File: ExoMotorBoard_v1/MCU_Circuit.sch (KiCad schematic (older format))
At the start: 11 parts, among them IC1 DSPIC33FJ128MC802-I_SP, SW1 SW_Push_Dual

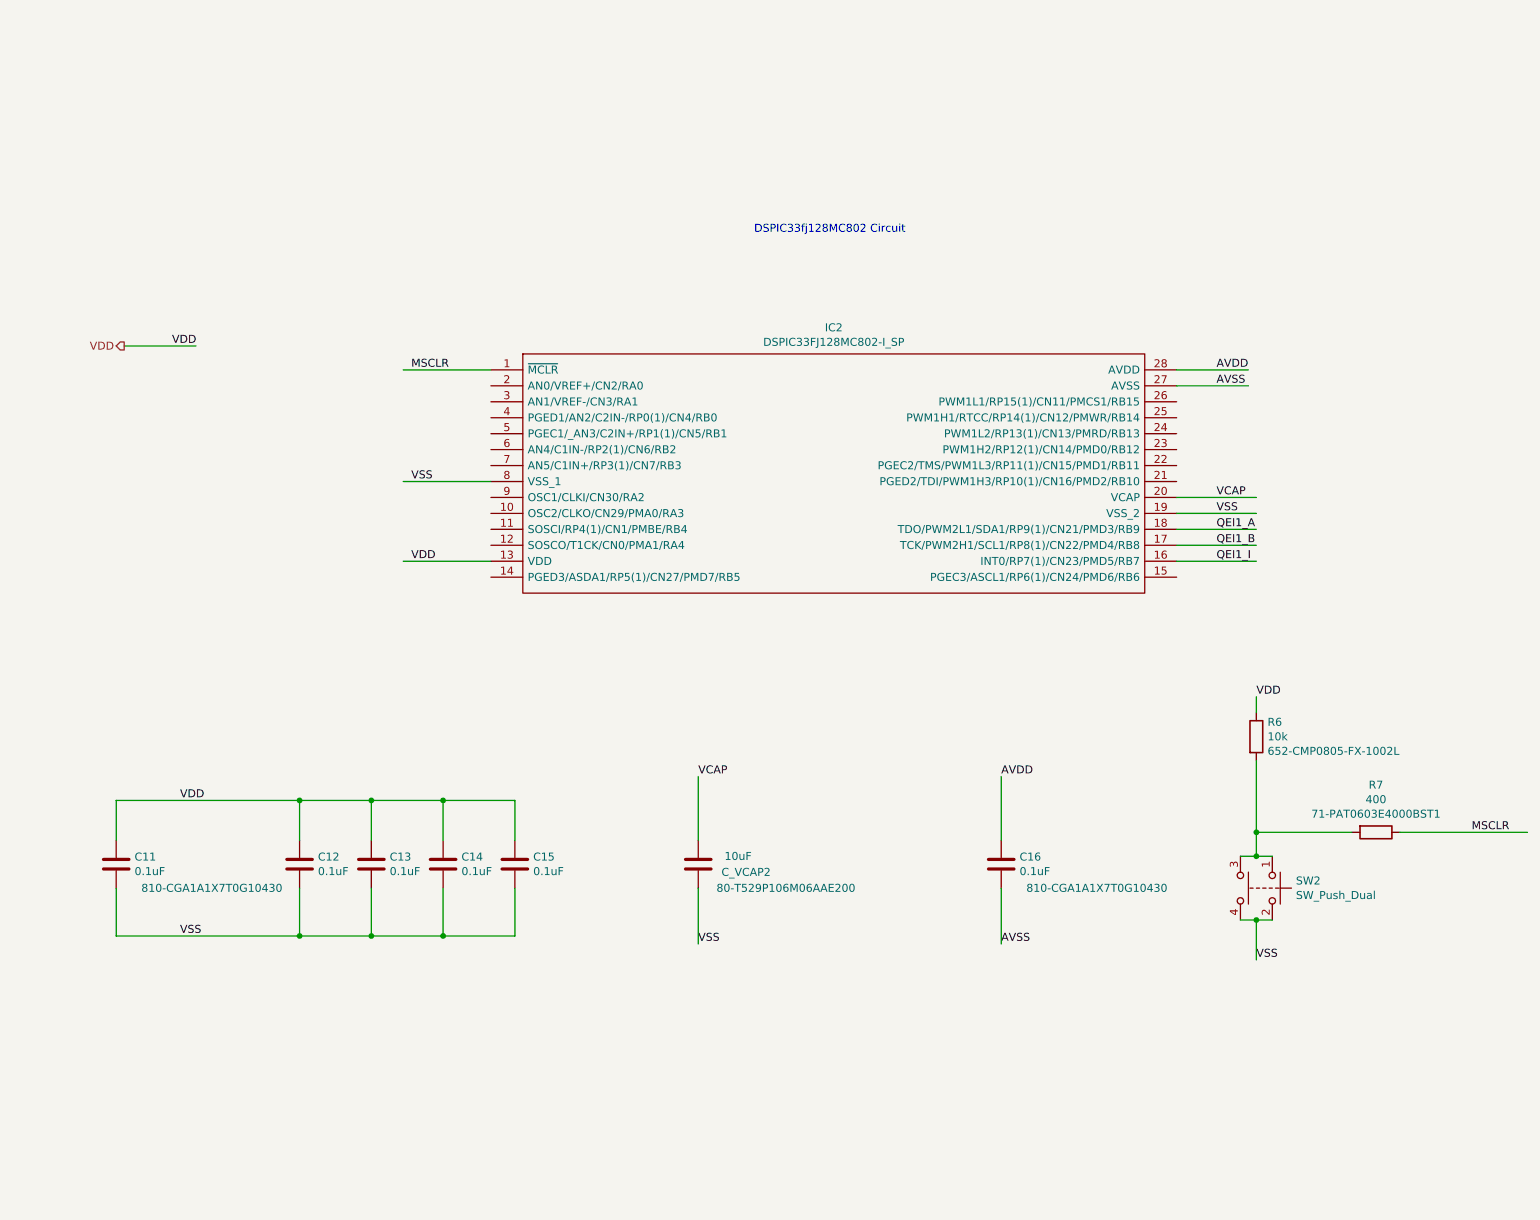
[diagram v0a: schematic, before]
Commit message: MCU schematic connections updated
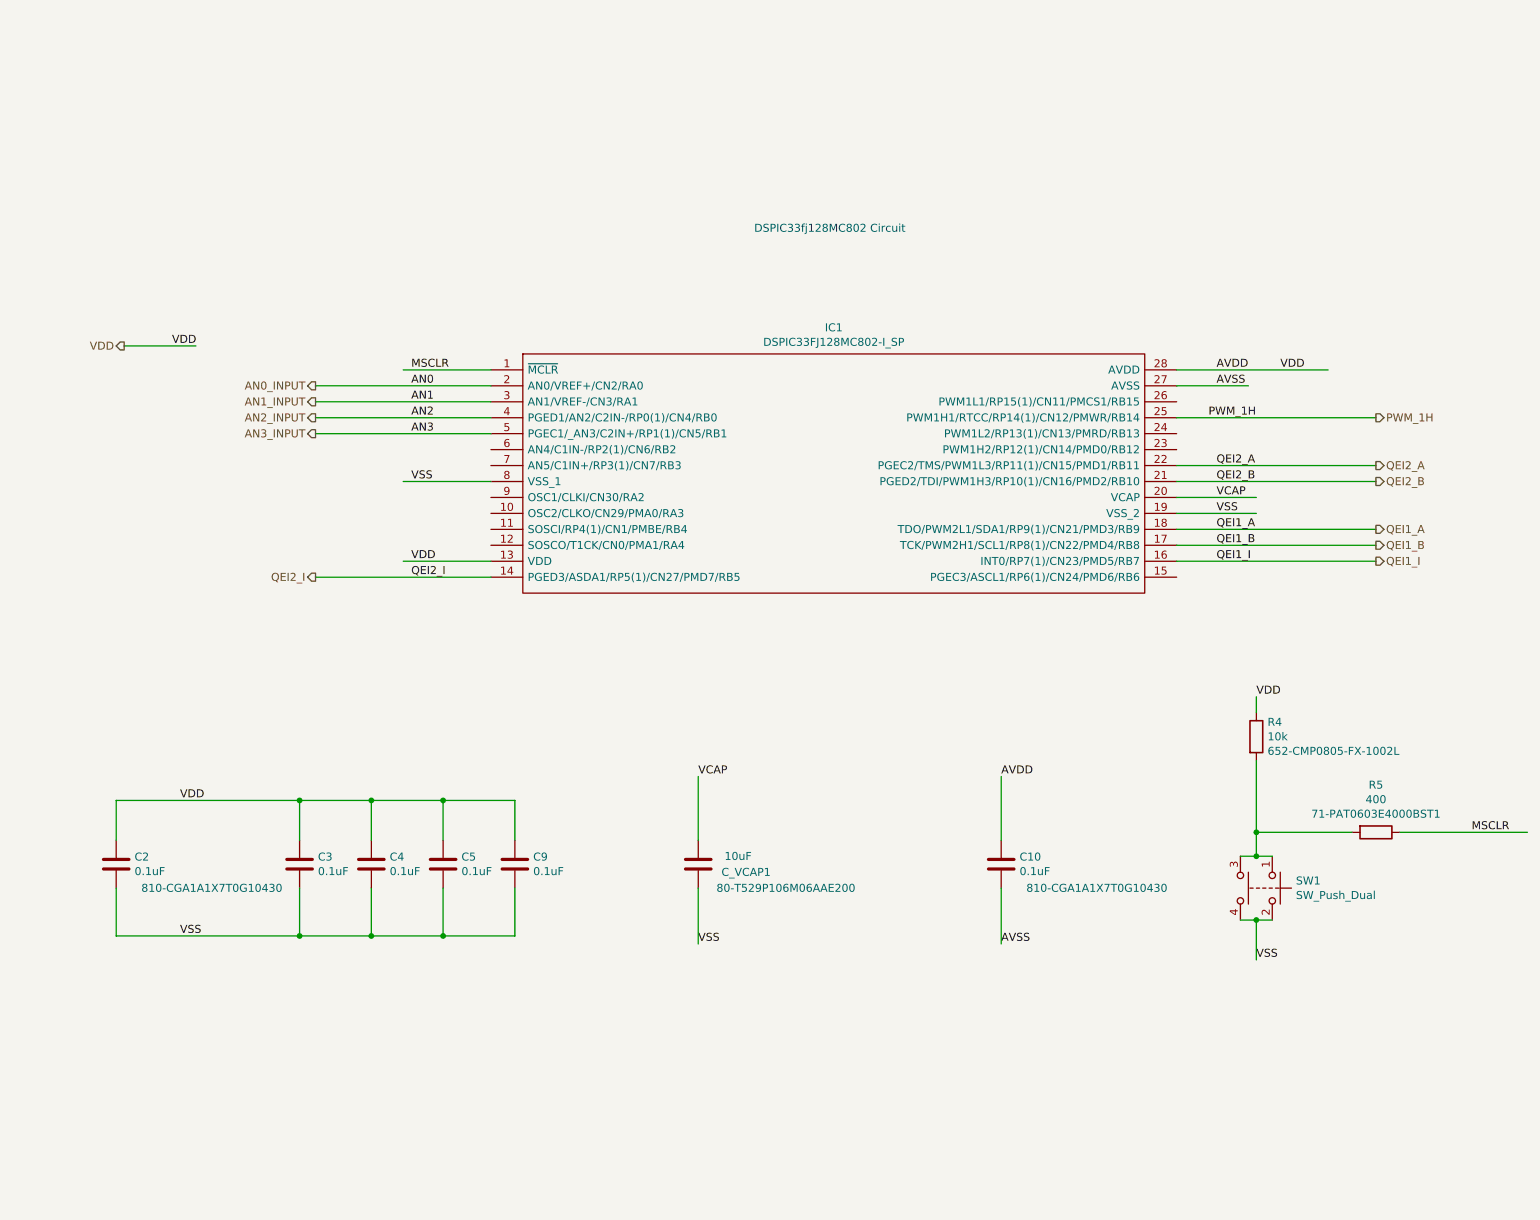
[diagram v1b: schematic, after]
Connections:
- net labels added: AN0, AN0_INPUT, AN1, AN1_INPUT, AN2, AN2_INPUT, AN3, AN3_INPUT, PWM_1H, QEI2_A, QEI2_B, QEI2_I
- wire segments 43 -> 51
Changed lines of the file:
@@
 $Descr A4 11693 8268
 encoding utf-8
-Sheet 8 8
+Sheet 2 8
 Title ""
 Date ""
@@
 AR Path="/610E570F/610E8175" Ref="IC1"  Part="1"
 AR Path="/6118F320/610E8175" Ref="IC2"  Part="1"
-F 0 "IC2" H 5950 2615 50  0000 C CNN
+F 0 "IC1" H 5950 2615 50  0000 C CNN
 F 1 "DSPIC33FJ128MC802-I_SP" H 5950 2524 50  0000 C CNN
 F 2 "DSPIC33FJ128MC802-I_SP:DIP794W56P254L3486H508Q28N" H 7950 2450 50  0001 L CNN
@@
 AR Path="/610E570F/610E817B" Ref="C_VCAP1"  Part="1"
 AR Path="/6118F320/610E817B" Ref="C_VCAP2"  Part="1"
-F 0 "C_VCAP2" H 4800 5500 50  0000 C CNN
+F 0 "C_VCAP1" H 4800 5500 50  0000 C CNN
 F 1 "10uF" H 4850 5400 50  0000 C CNN
 F 2 "Capacitor_SMD:C_0805_2012Metric_Pad1.18x1.45mm_HandSolder" H 5138 5300 50  0001 C CNN
@@
 AR Path="/610E570F/610E818F" Ref="C2"  Part="1"
 AR Path="/6118F320/610E818F" Ref="C11"  Part="1"
-F 0 "C11" H 1565 5496 50  0000 L CNN
+F 0 "C2" H 1565 5496 50  0000 L CNN
 F 1 "0.1uF" H 1565 5405 50  0000 L CNN
 F 2 "Capacitor_SMD:C_0805_2012Metric_Pad1.18x1.45mm_HandSolder" H 1488 5300 50  0001 C CNN
@@
 AR Path="/610E570F/61167308" Ref="C3"  Part="1"
 AR Path="/6118F320/61167308" Ref="C12"  Part="1"
-F 0 "C12" H 2715 5496 50  0000 L CNN
+F 0 "C3" H 2715 5496 50  0000 L CNN
 F 1 "0.1uF" H 2715 5405 50  0000 L CNN
 F 2 "Capacitor_SMD:C_0805_2012Metric_Pad1.18x1.45mm_HandSolder" H 2638 5300 50  0001 C CNN
@@
 AR Path="/610E570F/611683F9" Ref="C4"  Part="1"
 AR Path="/6118F320/611683F9" Ref="C13"  Part="1"
-F 0 "C13" H 3165 5496 50  0000 L CNN
+F 0 "C4" H 3165 5496 50  0000 L CNN
 F 1 "0.1uF" H 3165 5405 50  0000 L CNN
 F 2 "Capacitor_SMD:C_0805_2012Metric_Pad1.18x1.45mm_HandSolder" H 3088 5300 50  0001 C CNN
@@
 AR Path="/610E570F/61168710" Ref="C5"  Part="1"
 AR Path="/6118F320/61168710" Ref="C14"  Part="1"
-F 0 "C14" H 3615 5496 50  0000 L CNN
+F 0 "C5" H 3615 5496 50  0000 L CNN
 F 1 "0.1uF" H 3615 5405 50  0000 L CNN
 F 2 "Capacitor_SMD:C_0805_2012Metric_Pad1.18x1.45mm_HandSolder" H 3538 5300 50  0001 C CNN
@@
 AR Path="/610E570F/61168A37" Ref="C9"  Part="1"
 AR Path="/6118F320/61168A37" Ref="C15"  Part="1"
-F 0 "C15" H 4065 5496 50  0000 L CNN
+F 0 "C9" H 4065 5496 50  0000 L CNN
 F 1 "0.1uF" H 4065 5405 50  0000 L CNN
 F 2 "Capacitor_SMD:C_0805_2012Metric_Pad1.18x1.45mm_HandSolder" H 3988 5300 50  0001 C CNN
@@
 	5100 5600 5100 5950
 Wire Wire Line
-	8550 2350 8100 2350
-Wire Wire Line
 	8100 2450 8550 2450
 Text Label 8350 2350 0    50   ~ 0
@@
 AR Path="/610E570F/61184548" Ref="C10"  Part="1"
 AR Path="/6118F320/61184548" Ref="C16"  Part="1"
-F 0 "C16" H 7115 5496 50  0000 L CNN
+F 0 "C10" H 7115 5496 50  0000 L CNN
 F 1 "0.1uF" H 7115 5405 50  0000 L CNN
 F 2 "Capacitor_SMD:C_0805_2012Metric_Pad1.18x1.45mm_HandSolder" H 7038 5300 50  0001 C CNN
@@
 Text Label 3300 2350 0    50   ~ 0
 MSCLR
-Wire Wire Line
-	8100 3350 8600 3350
-Wire Wire Line
-	8100 3450 8600 3450
-Wire Wire Line
-	8100 3550 8600 3550
 Text Label 8350 3350 0    50   ~ 0
 QEI1_A
@@
 AR Path="/610E570F/611A30AE" Ref="R4"  Part="1"
 AR Path="/6118F320/611A30AE" Ref="R6"  Part="1"
-F 0 "R6" H 8670 4741 50  0000 L CNN
+F 0 "R4" H 8670 4741 50  0000 L CNN
 F 1 "10k" H 8670 4650 50  0000 L CNN
 F 2 "Resistor_SMD:R_0805_2012Metric_Pad1.20x1.40mm_HandSolder" V 8530 4650 50  0001 C CNN
@@
 AR Path="/610E570F/611A34F1" Ref="R5"  Part="1"
 AR Path="/6118F320/611A34F1" Ref="R7"  Part="1"
-F 0 "R7" V 9053 5250 50  0000 C CNN
+F 0 "R5" V 9053 5250 50  0000 C CNN
 F 1 "400" V 9144 5250 50  0000 C CNN
 F 2 "Resistor_SMD:R_0603_1608Metric_Pad0.98x0.95mm_HandSolder" V 9280 5250 50  0001 C CNN
@@
 AR Path="/610E570F/611A7040" Ref="SW1"  Part="1"
 AR Path="/6118F320/611A7040" Ref="SW2"  Part="1"
-F 0 "SW2" V 8654 5748 50  0000 L CNN
+F 0 "SW1" V 8654 5748 50  0000 L CNN
 F 1 "SW_Push_Dual" V 8745 5748 50  0000 L CNN
 F 2 "Button_Switch_THT:SW_PUSH_6mm_H5mm" H 8700 5800 50  0001 C CNN
@@
 Wire Wire Line
 	9500 5250 10300 5250
+Text Label 8350 2950 0    50   ~ 0
+QEI2_A
+Text Label 8350 3050 0    50   ~ 0
+QEI2_B
+Text Label 3300 3650 0    50   ~ 0
+QEI2_I
+Text Label 8300 2650 0    50   ~ 0
+PWM_1H
+Text Label 3300 2450 0    50   ~ 0
+AN0
+Text Label 3300 2550 0    50   ~ 0
+AN1
+Text Label 3300 2650 0    50   ~ 0
+AN2
+Text Label 3300 2750 0    50   ~ 0
+AN3
+Wire Wire Line
+	8100 2350 9050 2350
+Text Label 8750 2350 0    50   ~ 0
+VDD
+Text HLabel 9350 3550 2    50   Output ~ 0
+QEI1_I
+Text HLabel 9350 3450 2    50   Output ~ 0
+QEI1_B
+Text HLabel 9350 3350 2    50   Output ~ 0
+QEI1_A
+Text HLabel 9350 3050 2    50   Output ~ 0
+QEI2_B
+Text HLabel 9350 2950 2    50   Output ~ 0
+QEI2_A
+Text HLabel 9350 2650 2    50   Output ~ 0
+PWM_1H
+Text HLabel 2700 3650 0    50   Output ~ 0
+QEI2_I
+Wire Wire Line
+	8100 2650 9350 2650
+Wire Wire Line
+	8100 2950 9350 2950
+Wire Wire Line
+	8100 3050 9350 3050
+Wire Wire Line
+	8100 3350 9350 3350
+Wire Wire Line
+	8100 3450 9350 3450
+Wire Wire Line
+	8100 3550 9350 3550
+Wire Wire Line
+	2700 3650 3800 3650
+Text HLabel 2700 2750 0    50   Output ~ 0
+AN3_INPUT
+Text HLabel 2700 2650 0    50   Output ~ 0
+AN2_INPUT
+Text HLabel 2700 2550 0    50   Output ~ 0
+AN1_INPUT
+Text HLabel 2700 2450 0    50   Output ~ 0
+AN0_INPUT
+Wire Wire Line
+	2700 2450 3800 2450
+Wire Wire Line
+	2700 2550 3800 2550
+Wire Wire Line
+	2700 2650 3800 2650
+Wire Wire Line
+	2700 2750 3800 2750
 $EndSCHEMATC

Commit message: MCU connection updated
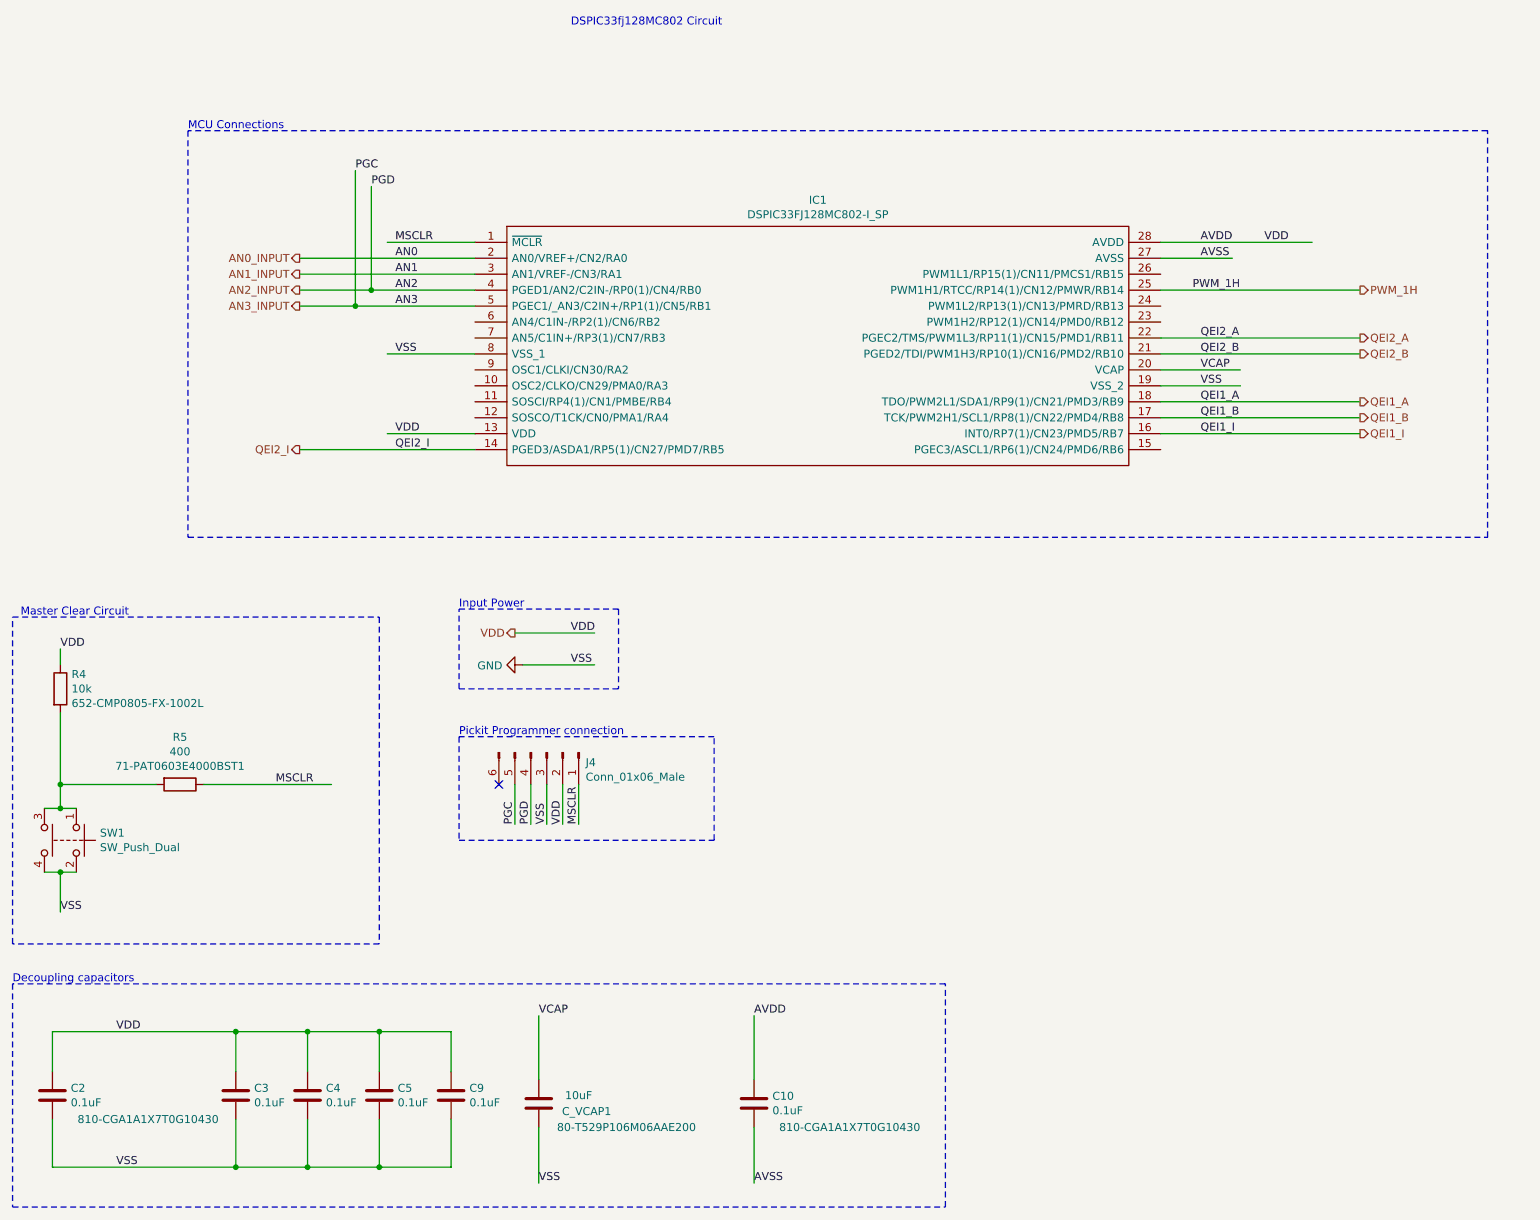
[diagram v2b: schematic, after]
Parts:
- added J4: Conn_01x06_Male, Connector_PinHeader_1.27mm:PinHeader_1x06_P1.27mm_Vertical, symbol Connector:Conn_01x06_Male
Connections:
- net labels added: GND, PGC, PGD
- wire segments 51 -> 61
- no-connect marks 0 -> 1
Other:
- note added: "Decoupling capacitors\n"
- note added: "Input Power\n"
- note added: "MCU Connections\n"
- note added: "Master Clear Circuit\n"
- note added: "Pickit Programmer connection\n"
- moved on the sheet: C10, C2, C3, C4, C5, C9, C_VCAP1, IC1, R4, R5, SW1

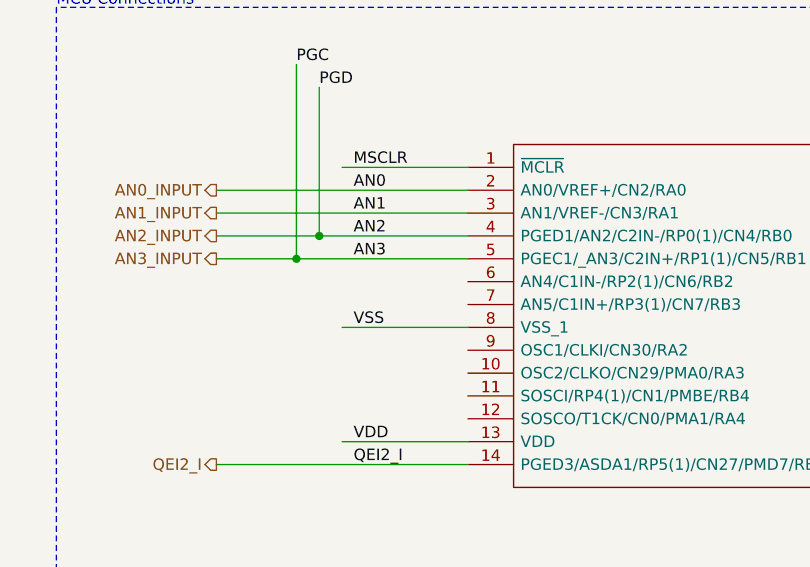
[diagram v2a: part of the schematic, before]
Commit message: UART1 Connections added in MCU
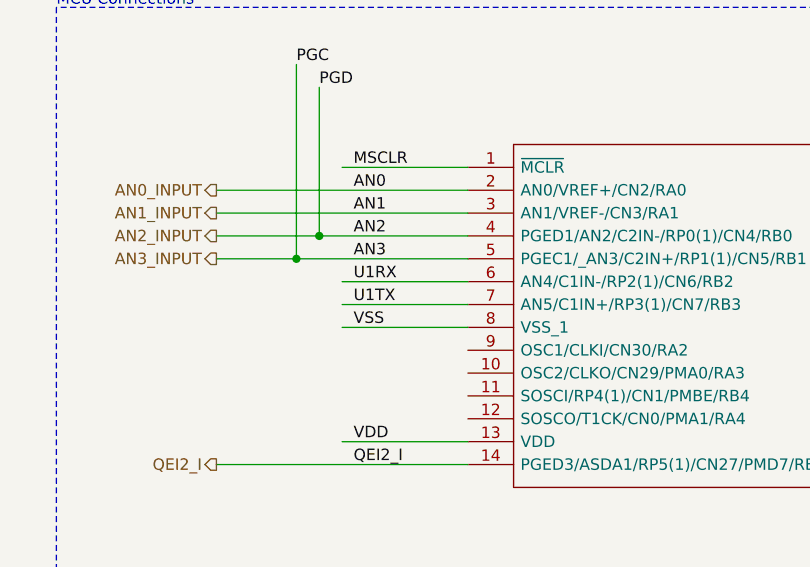
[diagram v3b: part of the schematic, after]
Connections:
- net labels added: U1RX, U1TX
- wire segments 61 -> 63
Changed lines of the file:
@@
 AR Path="/610E570F/611C897C" Ref="#PWR0102"  Part="1"
 AR Path="/6118F320/611C897C" Ref="#PWR0104"  Part="1"
-F 0 "#PWR0104" H 4000 3950 50  0001 C CNN
+F 0 "#PWR0102" H 4000 3950 50  0001 C CNN
 F 1 "GND" V 4005 4072 50  0000 R CNN
 F 2 "" H 4000 4200 50  0001 C CNN
@@
 Text Notes 1900 850  0    50   ~ 0
 MCU Connections\n
+Wire Wire Line
+	3700 2050 3150 2050
+Wire Wire Line
+	3700 2150 3150 2150
+Text Label 3200 2050 0    50   ~ 0
+U1RX
+Text Label 3200 2150 0    50   ~ 0
+U1TX
 $EndSCHEMATC
